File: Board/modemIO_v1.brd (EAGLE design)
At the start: 100 x 80 mm, 24 parts, among them IC1 TLV320AIC14R-PDSO-G30, IC2 SN74LVC04ADRR-PDSO-G14, Q1-18.432MHZ ASFL1

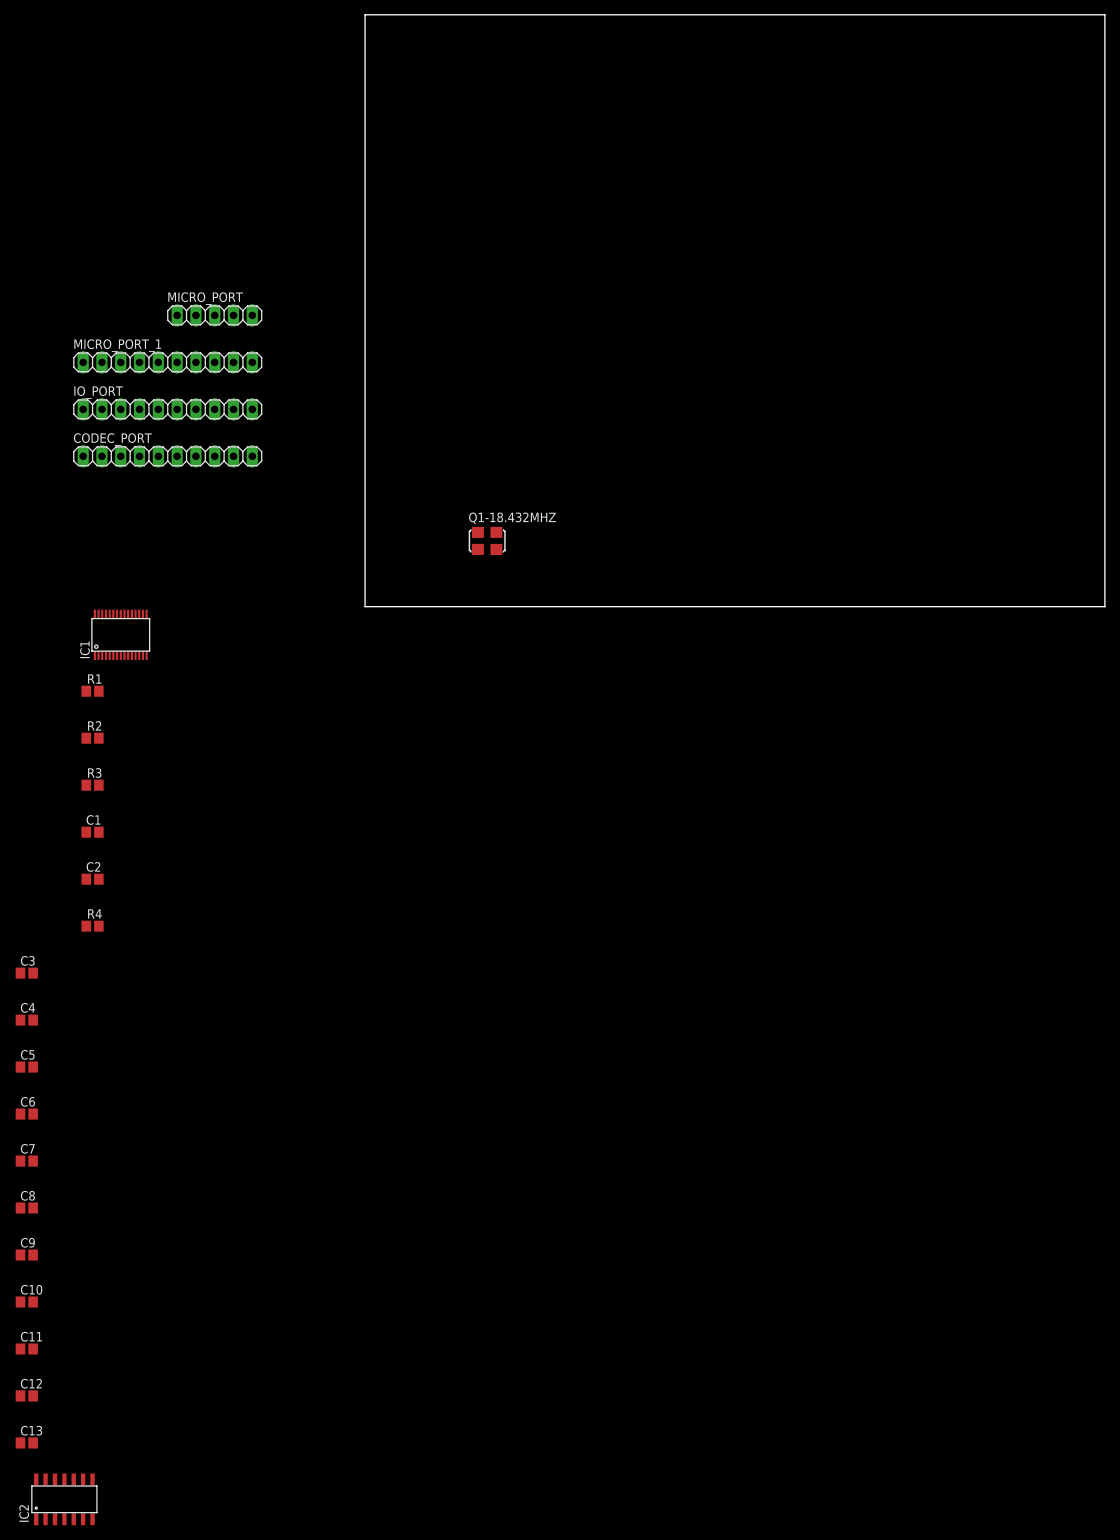
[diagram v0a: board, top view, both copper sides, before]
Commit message: + pull up to AMBE's Reset & progress in ModemIO brd
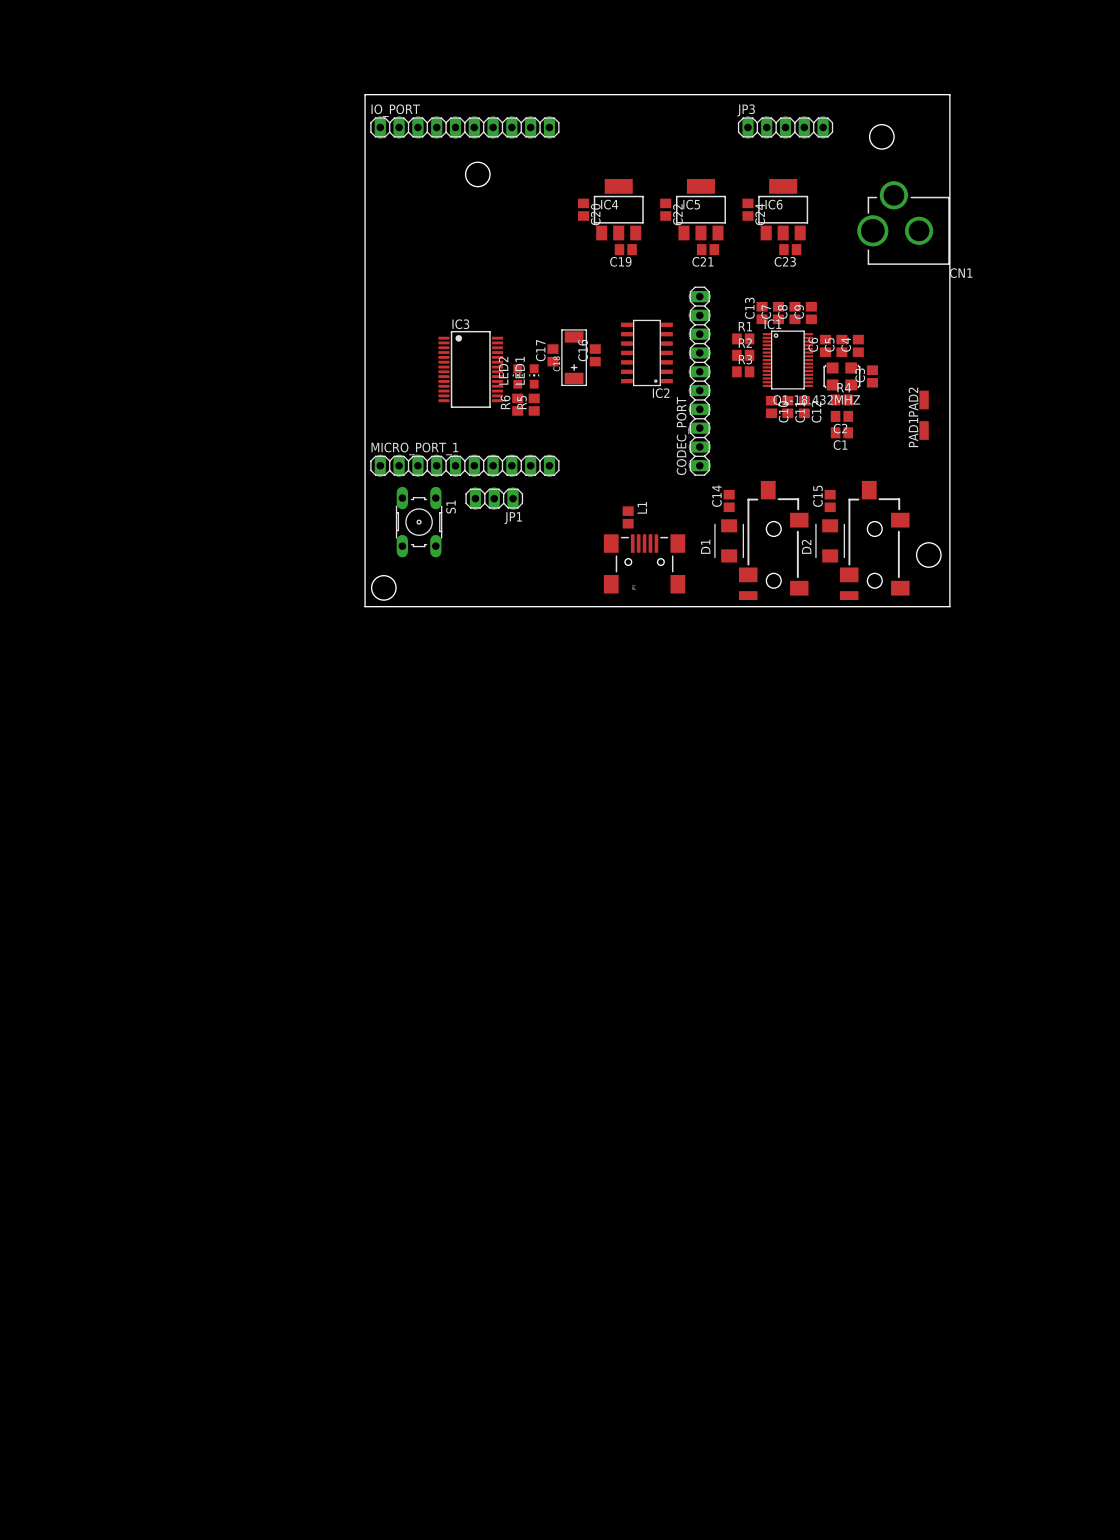
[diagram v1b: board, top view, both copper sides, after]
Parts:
- removed MICRO_PORT: (no value), pinhead:1X05
- added C14: C10uF 6.3V, resistor:C0805
- added C15, C16, C17: C0.1uF 10V, resistor:C0805
- added C18: C4.7uF 10V, OPL Eagle Library:AVX-C
- added C19, C20, C21, C22, C23, C24: C1uF 10V, resistor:C0805
- added CN1: (no value), adafruit:DCJACK_2MM_PTH
- added D1, D2: SMBJ10CA, diode:SMBJ
- added IC3: FT232RL, ftdichip:SSOP28
- added IC4, IC6: LD117AS33TR, v-reg:SOT223
- added IC5: LD117AS18TR, v-reg:SOT223
- added JP1: (no value), pinhead:1X03
- added JP2: USBSMD, SparkFun-Connectors:USB-MINIB
- added JP3: (no value), pinhead:1X05
- added L1: (no value), dp_devices:FB603
- added LED1, LED2: (no value), led:CHIP-LED0805
- added PAD1, PAD2: (no value), wirepad:SMD1,27-2,54
- added R5, R6: R1K, resistor:R0805
- added S1: (no value), switch-omron:B3F-10XX
- added U1, U2: (no value), SparkFun-Connectors:AUDIO-JACK-3.5MM-SMD
- moved C13 182.2 mm to (53.7, 39.7), turned to 90 degrees
- moved IC2 173.8 mm to (38.1, 34.3), turned to 90 degrees
- moved C12 170.0 mm to (59.4, 27.0), turned to 270 degrees
- moved C9 165.7 mm to (60.3, 39.7), turned to 90 degrees
- moved C11 163.7 mm to (57.1, 27.0), turned to 270 degrees
- moved C8 159.4 mm to (58.1, 39.7), turned to 90 degrees
- moved C10 157.4 mm to (54.9, 27.0), turned to 270 degrees
- moved C7 153.2 mm to (55.9, 39.7), turned to 90 degrees
- moved C6 149.8 mm to (62.2, 35.2), turned to 90 degrees
- moved C5 147.1 mm to (64.5, 35.2), turned to 90 degrees
- moved C4 144.7 mm to (66.7, 35.2), turned to 90 degrees
- moved C3 139.9 mm to (68.6, 31.1), turned to 90 degrees
- moved R4 123.8 mm to (64.5, 27.9)
- moved C2 119.0 mm to (64.5, 25.7), turned to 180 degrees
- moved C1 114.8 mm to (64.5, 23.5), turned to 180 degrees
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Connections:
- removed net CONFIG10: MICRO_PORT_1.4
- removed net CONFIG11: MICRO_PORT_1.5
- removed net CONFIG12: MICRO_PORT_1.6
- removed net CONFIG13: MICRO_PORT_1.7
- removed net CONFIG14: MICRO_PORT_1.8
- removed net CONFIG15: MICRO_PORT_1.9
- removed net CONFIG8: MICRO_PORT_1.2
- removed net CONFIG9: MICRO_PORT_1.3
- removed net RXRDY: MICRO_PORT.4
- removed net RXRQST: MICRO_PORT.3
- removed net TXFRM: MICRO_PORT.5
- removed net TXRDY: MICRO_PORT.2
- removed net TXRQST: MICRO_PORT.1
- new net 3V3OUT: C16.1, IC3.17, JP1.1
- new net 5V: C17.1, C18.+, IC3.20, JP1.3, L1.1, R5.1, R6.1
- new net 5V_USB: JP2.VBUS, L1.2
- new net DC_IN: C19.1, C21.1, C23.1, CN1.PWR, IC4.3, IC5.3, IC6.3
- new net N$1: C14.1, D1.C, U1.RING
- new net N$2: IC3.23, LED1.C
- new net N$4: IC3.22, LED2.C
- new net N$5: C15.1, D2.C, U2.RING
- new net N$6: LED1.A, R5.2
- new net N$9: LED2.A, R6.2
- new net USBDM: IC3.16, JP2.D-
- new net USBDP: IC3.15, JP2.D+
- new net VCCIO: IC3.4, JP1.2
- net 1V8: now also C22.1, IC5.4
- net 3V3: now also C20.1, IC4.4
- net 3V3A: now also C24.1, IC6.4
- net AGND: now also C23.2, C24.2, D1.A, D2.A, IC6.1, PAD2.1, U1.SLEEVE, U2.SLEEVE
- net ANALOG_IN_2: now also C15.2
- net ANALOG_OUTP1: now also C14.2
- net DSP_RESET: now also S1.3, S1.4
- net GND: now also C16.2, C17.2, C18.-, C19.2, C20.2, C21.2, C22.2, C4.2, CN1.GND, CN1.GNDBREAK, IC3.18, IC3.21, IC3.25, IC3.26, IC3.7, IC4.1, IC5.1, JP2.GND, JP3.5, MICRO_PORT_1.10, MICRO_PORT_1.2, MICRO_PORT_1.3, MICRO_PORT_1.4, MICRO_PORT_1.5, MICRO_PORT_1.6, MICRO_PORT_1.7, MICRO_PORT_1.8, MICRO_PORT_1.9, PAD1.1, S1.1, S1.2
- net STAT2/UART0_RTS: now also IC3.3, JP3.4
- net UART0_CHAN_RX: now also IC3.5, JP3.1
- net UART0_CHAN_TX: now also IC3.1, JP3.2
- net UART0_CTS: now also IC3.11, JP3.3
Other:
- board size 100 x 80 mm -> 79 x 69.2 mm

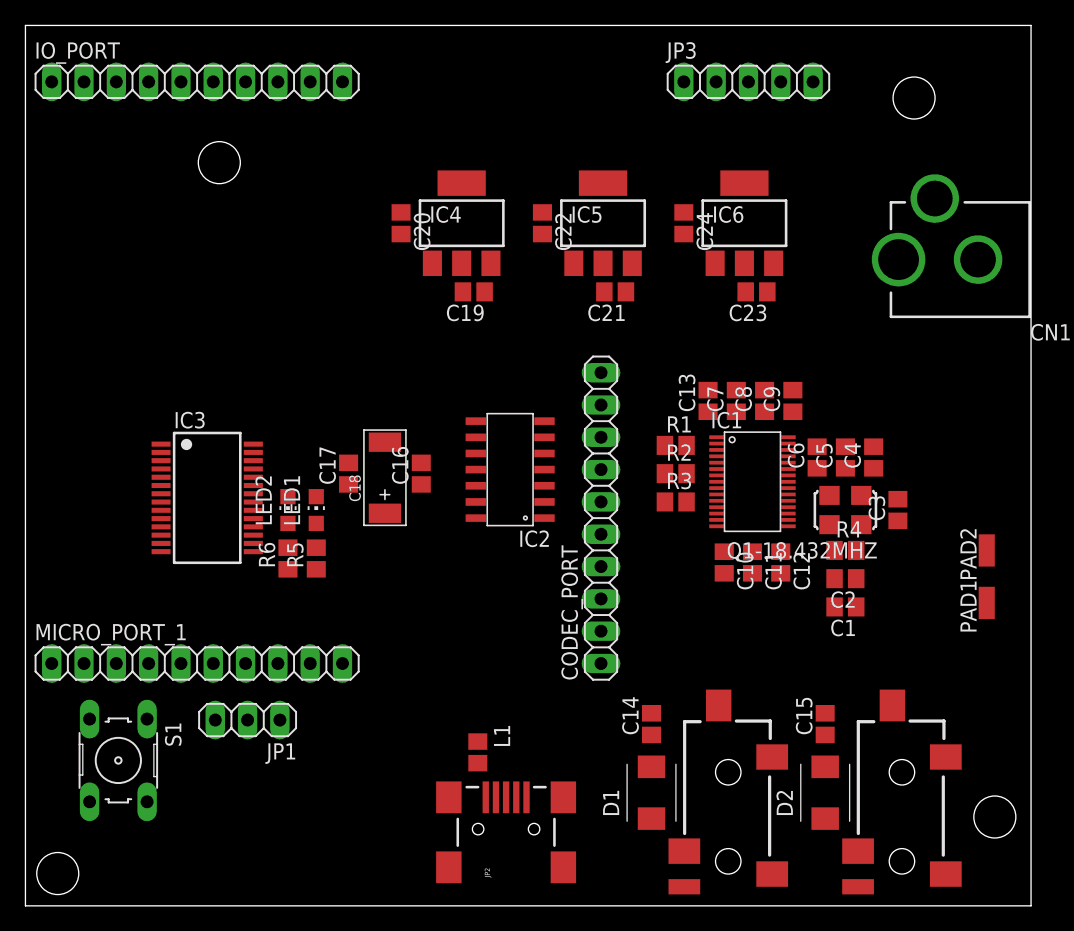
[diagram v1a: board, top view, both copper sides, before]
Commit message: Finish routing modemIO board
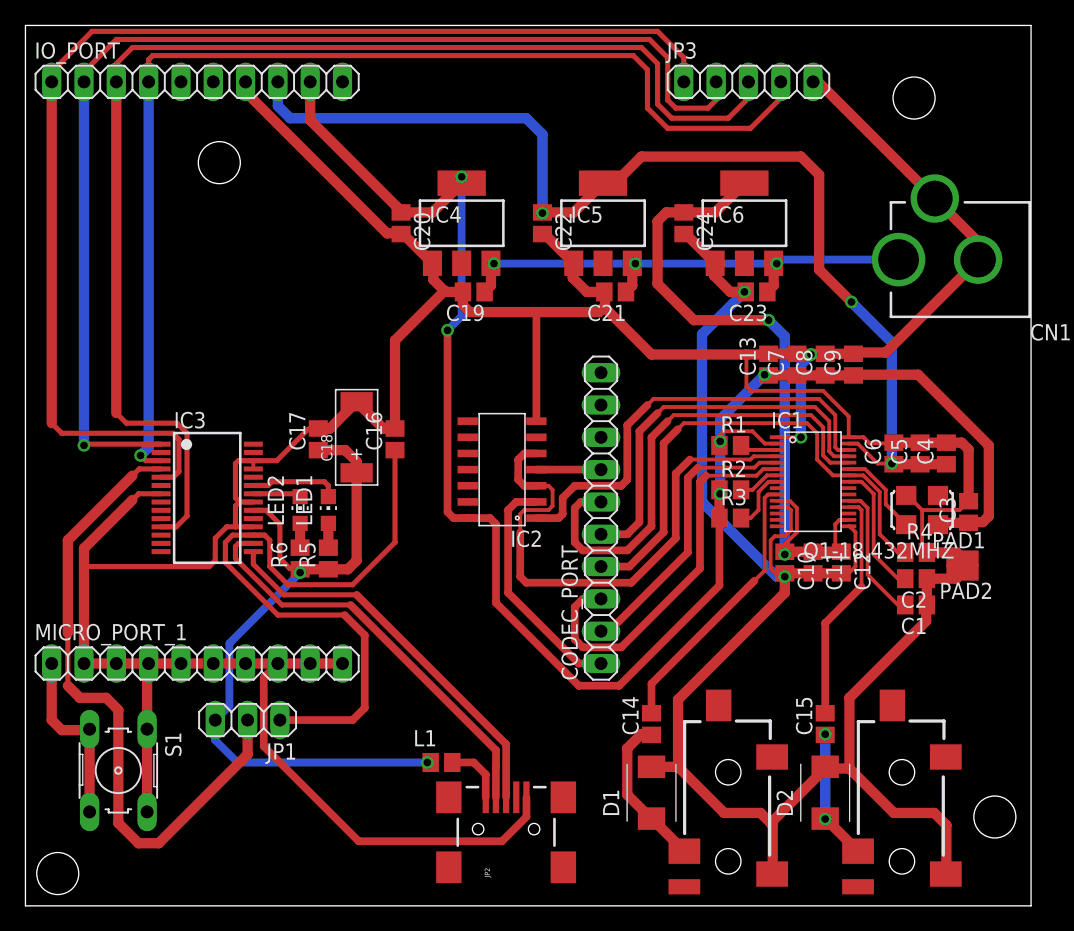
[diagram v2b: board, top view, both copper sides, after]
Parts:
- moved C6 6.04 mm to (68.3, 35.6)
- moved Q1-18.432MHZ 6.03 mm to (70.5, 31.1)
- moved C5 5.88 mm to (70.3, 35.6)
- moved C4 5.72 mm to (72.4, 35.6)
- moved C1 5.56 mm to (70.0, 23.7)
- moved C3 5.56 mm to (74.1, 31.0)
- moved R4 5.56 mm to (70.0, 27.8)
- moved C2 5.56 mm to (70.0, 25.7)
- moved C13 5.55 mm to (58.4, 42.5)
- moved C8 5.55 mm to (62.9, 42.5)
- moved C9 5.55 mm to (65.1, 42.5)
- moved C7 5.55 mm to (60.6, 42.5)
- moved C11 4.76 mm to (61.9, 27.0)
- moved C12 4.76 mm to (64.1, 27.0)
- moved IC1 4.76 mm to (61.9, 33.3)
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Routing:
- net GND: track 0.00 -> 289.0 mm, vias 0 -> 2
- net 3V3: track 0.00 -> 134.2 mm, vias 0 -> 5
- net AGND: track 0.00 -> 127.6 mm, vias 0 -> 2
- net UART0_CTS: track 0.00 -> 98.9 mm
- net UART0_CHAN_RX: track 0.00 -> 96.0 mm
- net UART0_CHAN_TX: track 0.00 -> 92.1 mm, vias 0 -> 1
- net STAT2/UART0_RTS: track 0.00 -> 89.4 mm, vias 0 -> 1
- net 1V8: track 0.00 -> 87.4 mm, vias 0 -> 3
- net 5V: track 0.00 -> 56.9 mm, vias 0 -> 2
- net 3V3A: track 0.00 -> 55.7 mm, vias 0 -> 2
- net 3V3OUT: track 0.00 -> 52.7 mm
- net VCCIO: track 0.00 -> 51.1 mm
- net CODEC_FS: track 0.00 -> 42.7 mm
- net DC_IN: track 0.00 -> 40.0 mm, vias 0 -> 3
- net CODEC_RESETN: track 0.00 -> 40.0 mm
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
